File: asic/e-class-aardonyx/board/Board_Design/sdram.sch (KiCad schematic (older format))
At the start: 27 parts, among them J4 Conn_1x4, U2 IS42S32160F-TSOP2, U3 CDCE913PW, Y2 27MHz

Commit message: update bom
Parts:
- U2: Description (none) -> IC DRAM 512M PARALLEL 86TSOP II; Digikey PartNumber (none) -> 706-1417-5-ND; Manufactured Part Number (none) -> IS42S32160F-7TLI; Maufaturer (none) -> ISSI, Integrated Silicon Solution Inc
- U3: Description (none) -> IC PROG PLL VCXO CLK SYN 14TSSOP; Digikey PartNumber (none) -> 296-38908-1-ND; Manufactured Part Number (none) -> CDCE913PWR; Maufaturer (none) -> Texas Instruments
- Y2: Description (none) -> CRYSTAL 27.0000MHZ 18PF SMD; Digikey PartNumber (none) -> XC1002CT-ND; Manufactured Part Number (none) -> ECS-270-18-5PX-F-TR; Maufaturer (none) -> ECS Inc.
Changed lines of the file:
@@
 F 1 "IS42S32160F-TSOP2" H 3050 4800 50  0000 C CNN
 F 2 "" H 3100 4950 50  0001 C CNN
-F 3 "" H 3100 4950 50  0001 C CNN
+F 3 "https://www.digikey.in/product-detail/en/issi-integrated-silicon-solution-inc/IS42S32160F-7TLI/706-1417-5-ND/5319838" H 3100 4950 50  0001 C CNN
+F 4 "IC DRAM 512M PARALLEL 86TSOP II" H 3100 4800 50  0001 C CNN "Description"
+F 5 "706-1417-5-ND" H 3100 4800 50  0001 C CNN "Digikey PartNumber"
+F 6 "IS42S32160F-7TLI" H 3100 4800 50  0001 C CNN "Manufactured Part Number"
+F 7 "ISSI, Integrated Silicon Solution Inc" H 3100 4800 50  0001 C CNN "Maufaturer"
 	1    3100 4800
 	1    0    0    -1
@@
 F 1 "27MHz" H 8650 1500 50  0000 L CNN
 F 2 "" H 8750 1350 50  0001 C CNN
-F 3 "~" H 8750 1350 50  0001 C CNN
+F 3 "https://www.digikey.in/product-detail/en/ecs-inc/ECS-270-18-5PX-F-TR/XC1002CT-ND/813243" H 8750 1350 50  0001 C CNN
+F 4 "CRYSTAL 27.0000MHZ 18PF SMD" H 8750 1350 50  0001 C CNN "Description"
+F 5 "XC1002CT-ND" H 8750 1350 50  0001 C CNN "Digikey PartNumber"
+F 6 "ECS-270-18-5PX-F-TR" H 8750 1350 50  0001 C CNN "Manufactured Part Number"
+F 7 "ECS Inc." H 8750 1350 50  0001 C CNN "Maufaturer"
 	1    8750 1350
 	-1   0    0    1
@@
 F 1 "CDCE913PW" H 9150 1350 50  0000 C CNN
 F 2 "SOP65P640X120-14N" H 8750 2200 50  0001 L BNN
-F 3 "CDCE913PW" H 8750 2200 50  0001 L BNN
+F 3 "https://www.digikey.in/product-detail/en/texas-instruments/CDCE913PWR/296-38908-1-ND/5143014" H 8750 2200 50  0001 L BNN
 F 4 "58M0317" H 8750 2200 50  0001 L BNN "Field4"
 F 5 "TSSOP-14" H 8750 2200 50  0001 L BNN "Field5"
 F 6 "Texas Instruments" H 8750 2200 50  0001 L BNN "Field6"
 F 7 "1543748" H 8750 2200 50  0001 L BNN "Field7"
+F 8 "IC PROG PLL VCXO CLK SYN 14TSSOP" H 8750 2200 50  0001 C CNN "Description"
+F 9 "296-38908-1-ND" H 8750 2200 50  0001 C CNN "Digikey PartNumber"
+F 10 "CDCE913PWR" H 8750 2200 50  0001 C CNN "Manufactured Part Number"
+F 11 "Texas Instruments" H 8750 2200 50  0001 C CNN "Maufaturer"
 	1    8750 2200
 	1    0    0    -1
@@
 F 1 "22E" V 9900 2750 50  0000 C CNN
 F 2 "" V 9990 2590 50  0001 C CNN
-F 3 "~" H 9950 2600 50  0001 C CNN
+F 3 "" H 9950 2600 50  0001 C CNN
 	1    9950 2600
 	0    1    1    0

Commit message: update BOM
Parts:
- C18, C19, C20, C21, C22, C23, C24, C25, C26, C27, C28, C29, C30, C31, C32: Description CAP CER 0.1UF 16V X7R 0402 -> CAP CER 0.1UF 25V X7R 0402; Digikey PartNumber 490-6328-1-ND -> 478-10050-1-ND; Manufactured Part Number GRM155R71C104KA88J -> 04023C104JAT2A; Maufaturer Murata -> AVX Corporation
- R24: Description (none) -> RES SMD 22 OHM 1% 1/16W 0402; Digikey PartNumber (none) -> 311-22.0LRCT-ND; Manufactured Part Number (none) -> RC0402FR-0722RL; Maufaturer (none) -> Yageo

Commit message: updated BOM
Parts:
- C18, C19, C20, C21, C22, C23, C24, C25, C26, C27, C28, C29: value 0.1uF -> 0.1UF,0402
- C30, C31, C32: value 0.1uf -> 0.1UF,0402
- J4: Description (none) -> CONN HEADER VERT 4POS 2.54MM; Digikey PartNumber (none) -> 609-3262-ND; Manufactured Part Number (none) -> 68000-404HLF; Maufaturer (none) -> Amphenol ICC (FCI)
- R19, R20, R21, R22, R23: value 4.7K -> 4.7KE, 0402
- R24: value 22E -> 22E,0402
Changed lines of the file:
@@
 EESchema Schematic File Version 4
-EELAYER 30 0
+LIBS:Aardonyx-cache
+EELAYER 29 0
 EELAYER END
 $Descr A4 11693 8268
@@
 P 1650 1400
 F 0 "C18" H 1650 1500 50  0000 L CNN
-F 1 "0.1uF" H 1650 1300 50  0000 L CNN
+F 1 "0.1UF,0402" H 1650 1300 50  0000 L CNN
 F 2 "" H 1650 1400 50  0001 C CNN
 F 3 "https://www.digikey.in/product-detail/en/avx-corporation/04023C104JAT2A/478-10050-1-ND/6564273" H 1650 1400 50  0001 C CNN
@@
 P 1900 1400
 F 0 "C19" H 1900 1500 50  0000 L CNN
-F 1 "0.1uF" H 1900 1300 50  0000 L CNN
+F 1 "0.1UF,0402" H 1900 1300 50  0000 L CNN
 F 2 "" H 1900 1400 50  0001 C CNN
 F 3 "https://www.digikey.in/product-detail/en/avx-corporation/04023C104JAT2A/478-10050-1-ND/6564273" H 1900 1400 50  0001 C CNN
@@
 P 2150 1400
 F 0 "C20" H 2150 1500 50  0000 L CNN
-F 1 "0.1uF" H 2150 1300 50  0000 L CNN
+F 1 "0.1UF,0402" H 2150 1300 50  0000 L CNN
 F 2 "" H 2150 1400 50  0001 C CNN
 F 3 "https://www.digikey.in/product-detail/en/avx-corporation/04023C104JAT2A/478-10050-1-ND/6564273" H 2150 1400 50  0001 C CNN
@@
 P 2400 1400
 F 0 "C21" H 2400 1500 50  0000 L CNN
-F 1 "0.1uF" H 2400 1300 50  0000 L CNN
+F 1 "0.1UF,0402" H 2400 1300 50  0000 L CNN
 F 2 "" H 2400 1400 50  0001 C CNN
 F 3 "https://www.digikey.in/product-detail/en/avx-corporation/04023C104JAT2A/478-10050-1-ND/6564273" H 2400 1400 50  0001 C CNN
@@
 P 2650 1400
 F 0 "C22" H 2650 1500 50  0000 L CNN
-F 1 "0.1uF" H 2650 1300 50  0000 L CNN
+F 1 "0.1UF,0402" H 2650 1300 50  0000 L CNN
 F 2 "" H 2650 1400 50  0001 C CNN
 F 3 "https://www.digikey.in/product-detail/en/avx-corporation/04023C104JAT2A/478-10050-1-ND/6564273" H 2650 1400 50  0001 C CNN
@@
 P 2900 1400
 F 0 "C23" H 2900 1500 50  0000 L CNN
-F 1 "0.1uF" H 2900 1300 50  0000 L CNN
+F 1 "0.1UF,0402" H 2900 1300 50  0000 L CNN
 F 2 "" H 2900 1400 50  0001 C CNN
 F 3 "https://www.digikey.in/product-detail/en/avx-corporation/04023C104JAT2A/478-10050-1-ND/6564273" H 2900 1400 50  0001 C CNN
@@
 P 3150 1400
 F 0 "C24" H 3150 1500 50  0000 L CNN
-F 1 "0.1uF" H 3150 1300 50  0000 L CNN
+F 1 "0.1UF,0402" H 3150 1300 50  0000 L CNN
 F 2 "" H 3150 1400 50  0001 C CNN
 F 3 "https://www.digikey.in/product-detail/en/avx-corporation/04023C104JAT2A/478-10050-1-ND/6564273" H 3150 1400 50  0001 C CNN
@@
 P 3400 1400
 F 0 "C25" H 3400 1500 50  0000 L CNN
-F 1 "0.1uF" H 3400 1300 50  0000 L CNN
+F 1 "0.1UF,0402" H 3400 1300 50  0000 L CNN
 F 2 "" H 3400 1400 50  0001 C CNN
 F 3 "https://www.digikey.in/product-detail/en/avx-corporation/04023C104JAT2A/478-10050-1-ND/6564273" H 3400 1400 50  0001 C CNN
@@
 P 3650 1400
 F 0 "C26" H 3650 1500 50  0000 L CNN
-F 1 "0.1uF" H 3650 1300 50  0000 L CNN
+F 1 "0.1UF,0402" H 3650 1300 50  0000 L CNN
 F 2 "" H 3650 1400 50  0001 C CNN
 F 3 "https://www.digikey.in/product-detail/en/avx-corporation/04023C104JAT2A/478-10050-1-ND/6564273" H 3650 1400 50  0001 C CNN
@@
 P 3900 1400
 F 0 "C27" H 3900 1500 50  0000 L CNN
-F 1 "0.1uF" H 3900 1300 50  0000 L CNN
+F 1 "0.1UF,0402" H 3900 1300 50  0000 L CNN
 F 2 "" H 3900 1400 50  0001 C CNN
 F 3 "https://www.digikey.in/product-detail/en/avx-corporation/04023C104JAT2A/478-10050-1-ND/6564273" H 3900 1400 50  0001 C CNN
@@
 P 4150 1400
 F 0 "C28" H 4150 1500 50  0000 L CNN
-F 1 "0.1uF" H 4150 1300 50  0000 L CNN
+F 1 "0.1UF,0402" H 4150 1300 50  0000 L CNN
 F 2 "" H 4150 1400 50  0001 C CNN
 F 3 "https://www.digikey.in/product-detail/en/avx-corporation/04023C104JAT2A/478-10050-1-ND/6564273" H 4150 1400 50  0001 C CNN
@@
 P 4400 1400
 F 0 "C29" H 4400 1500 50  0000 L CNN
-F 1 "0.1uF" H 4400 1300 50  0000 L CNN
+F 1 "0.1UF,0402" H 4400 1300 50  0000 L CNN
 F 2 "" H 4400 1400 50  0001 C CNN
 F 3 "https://www.digikey.in/product-detail/en/avx-corporation/04023C104JAT2A/478-10050-1-ND/6564273" H 4400 1400 50  0001 C CNN
@@
 AR Path="/5D8B37B8/5EFB4D01" Ref="R20"  Part="1"
 F 0 "R20" H 7150 2350 50  0000 L CNN
-F 1 "4.7K" H 7150 2050 50  0000 L CNN
+F 1 "4.7KE, 0402" H 7150 2050 50  0000 L CNN
 F 2 "" V 7190 2190 50  0001 C CNN
 F 3 "https://www.digikey.in/product-detail/en/yageo/RC0402JR-074K7L/311-4-7KJRTR-ND/726477" H 7150 2200 50  0001 C CNN
@@
 AR Path="/5D8B37B8/5EFB4D07" Ref="R19"  Part="1"
 F 0 "R19" H 6850 2350 50  0000 L CNN
-F 1 "4.7K" H 6850 2050 50  0000 L CNN
+F 1 "4.7KE, 0402" H 6850 2050 50  0000 L CNN
 F 2 "" V 6890 2190 50  0001 C CNN
 F 3 "https://www.digikey.in/product-detail/en/yageo/RC0402JR-074K7L/311-4-7KJRTR-ND/726477" H 6850 2200 50  0001 C CNN
@@
 AR Path="/5D8B37B8/5EFB4D13" Ref="C31"  Part="1"
 F 0 "C31" H 10000 2100 50  0000 L CNN
-F 1 "0.1uf" H 10000 1900 50  0000 L CNN
+F 1 "0.1UF,0402" H 10000 1900 50  0000 L CNN
 F 2 "" H 10000 2000 50  0001 C CNN
 F 3 "https://www.digikey.in/product-detail/en/avx-corporation/04023C104JAT2A/478-10050-1-ND/6564273" H 10000 2000 50  0001 C CNN
@@
 AR Path="/5D8B37B8/5EFB4D19" Ref="C32"  Part="1"
 F 0 "C32" H 10250 2100 50  0000 L CNN
-F 1 "0.1uf" H 10250 1900 50  0000 L CNN
+F 1 "0.1UF,0402" H 10250 1900 50  0000 L CNN
 F 2 "" H 10250 2000 50  0001 C CNN
 F 3 "https://www.digikey.in/product-detail/en/avx-corporation/04023C104JAT2A/478-10050-1-ND/6564273" H 10250 2000 50  0001 C CNN
@@
 AR Path="/5D8B37B8/5EFB4D80" Ref="R24"  Part="1"
 F 0 "R24" V 9900 2450 50  0000 C CNN
-F 1 "22E" V 9900 2750 50  0000 C CNN
+F 1 "22E,0402" V 9900 2750 50  0000 C CNN
 F 2 "" V 9990 2590 50  0001 C CNN
 F 3 "https://www.digikey.com/product-detail/en/yageo/RC0402FR-0722RL/311-22-0LRCT-ND/729509" H 9950 2600 50  0001 C CNN
@@
 AR Path="/5D8B37B8/5F80E136" Ref="R21"  Part="1"
 F 0 "R21" H 7400 2350 50  0000 L CNN
-F 1 "4.7K" H 7400 2100 50  0000 L CNN
+F 1 "4.7KE, 0402" H 7400 2100 50  0000 L CNN
 F 2 "" V 7440 2190 50  0001 C CNN
 F 3 "https://www.digikey.in/product-detail/en/yageo/RC0402JR-074K7L/311-4-7KJRTR-ND/726477" H 7400 2200 50  0001 C CNN
@@
 AR Path="/5D8B37B8/5F82D0FE" Ref="R23"  Part="1"
 F 0 "R23" H 7450 2800 50  0000 L CNN
-F 1 "4.7K" H 7650 2700 50  0000 L CNN
+F 1 "4.7KE, 0402" H 7650 2700 50  0000 L CNN
 F 2 "" V 7690 2790 50  0001 C CNN
 F 3 "https://www.digikey.in/product-detail/en/yageo/RC0402JR-074K7L/311-4-7KJRTR-ND/726477" H 7650 2800 50  0001 C CNN
@@
 AR Path="/5D8B37B8/5F8A4363" Ref="R22"  Part="1"
 F 0 "R22" H 7650 2150 50  0000 L CNN
-F 1 "4.7K" H 7700 1950 50  0000 L CNN
+F 1 "4.7KE, 0402" H 7700 1950 50  0000 L CNN
 F 2 "" V 7690 1990 50  0001 C CNN
 F 3 "https://www.digikey.in/product-detail/en/yageo/RC0402JR-074K7L/311-4-7KJRTR-ND/726477" H 7650 2000 50  0001 C CNN
@@
 AR Path="/5D8B37B8/5F8E5F7E" Ref="C30"  Part="1"
 F 0 "C30" H 7450 1650 50  0000 L CNN
-F 1 "0.1uf" H 7450 1450 50  0000 L CNN
+F 1 "0.1UF,0402" H 7450 1450 50  0000 L CNN
 F 2 "" H 7450 1550 50  0001 C CNN
 F 3 "https://www.digikey.in/product-detail/en/avx-corporation/04023C104JAT2A/478-10050-1-ND/6564273" H 7450 1550 50  0001 C CNN
@@
 F 1 "Conn_1x4" H 6200 2100 50  0000 L CNN
 F 2 "" H 6350 2450 50  0001 C CNN
-F 3 "~" H 6350 2450 50  0001 C CNN
+F 3 "https://www.digikey.com/product-detail/en/amphenol-icc-fci/68000-404HLF/609-3262-ND/1878463" H 6350 2450 50  0001 C CNN
+F 4 "CONN HEADER VERT 4POS 2.54MM" H 6350 2450 50  0001 C CNN "Description"
+F 5 "609-3262-ND" H 6350 2450 50  0001 C CNN "Digikey PartNumber"
+F 6 "68000-404HLF" H 6350 2450 50  0001 C CNN "Manufactured Part Number"
+F 7 "Amphenol ICC (FCI)" H 6350 2450 50  0001 C CNN "Maufaturer"
 	1    6350 2450
 	-1   0    0    -1

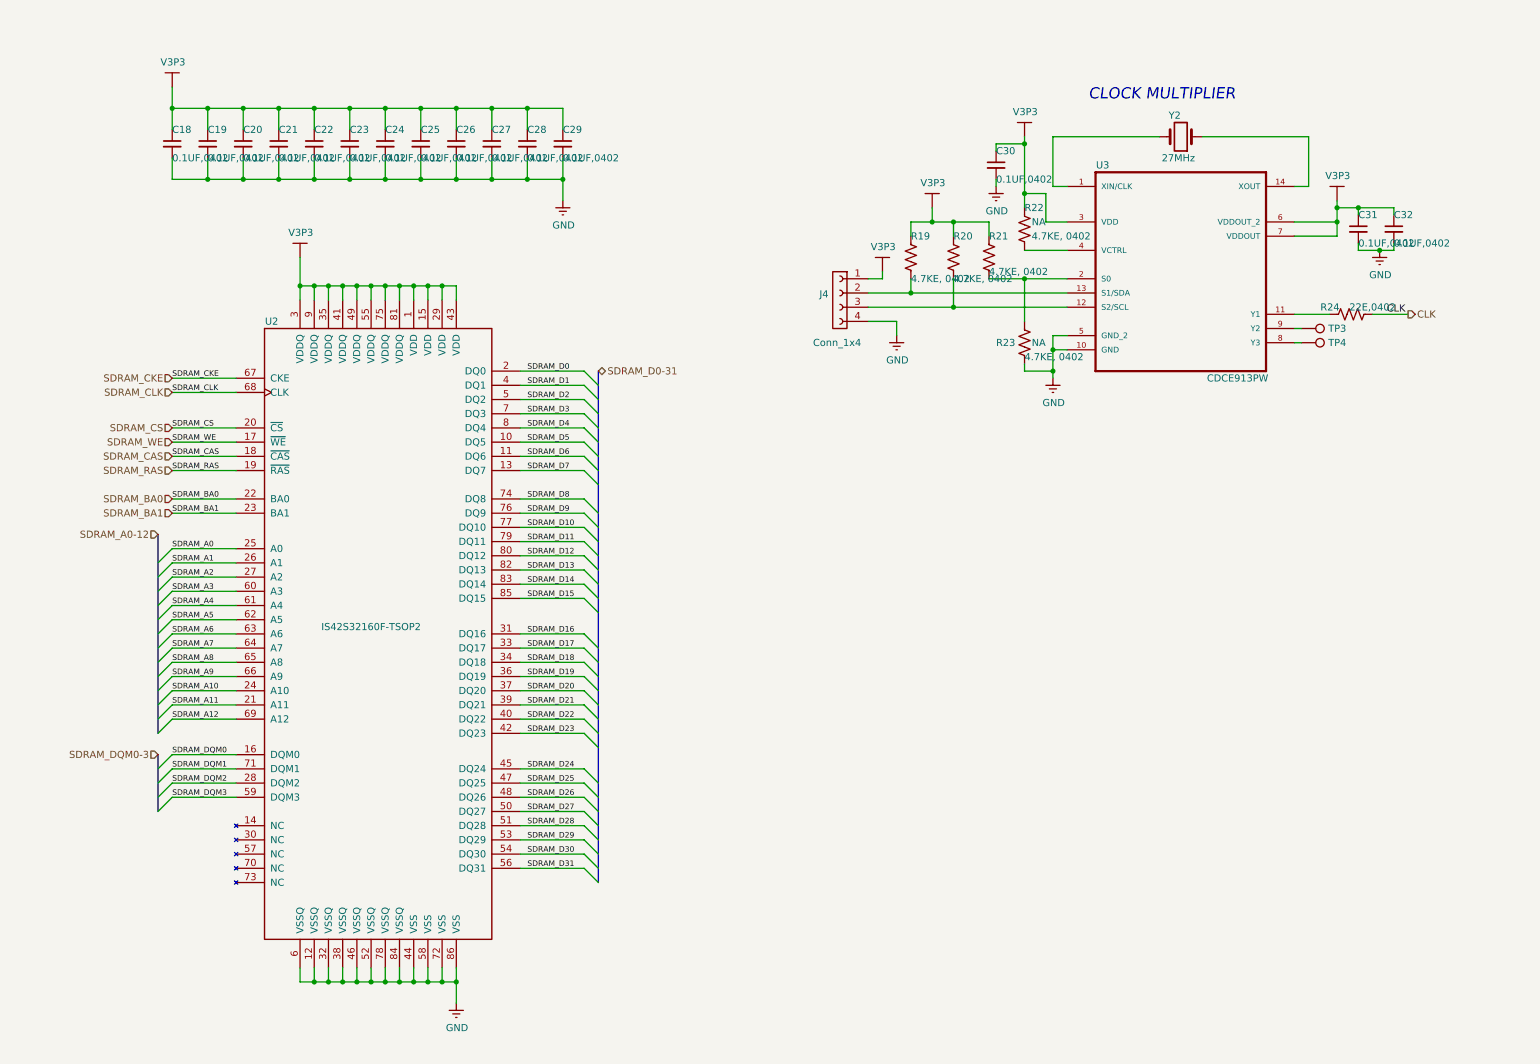
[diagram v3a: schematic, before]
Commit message: updated commented pending schematic
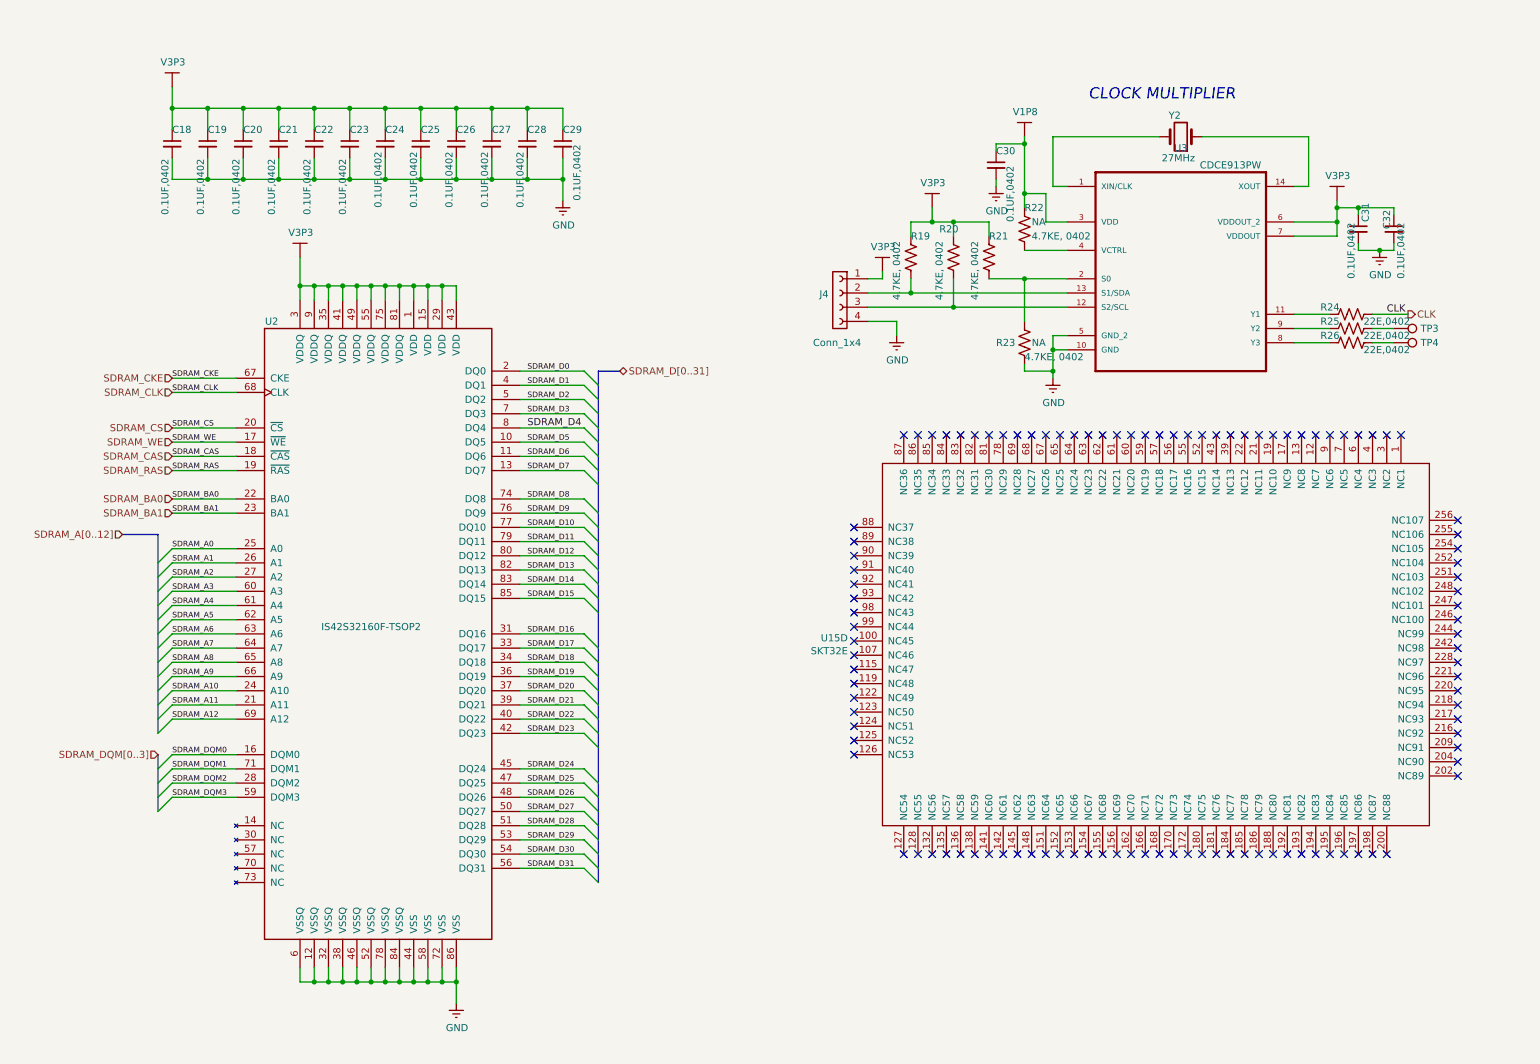
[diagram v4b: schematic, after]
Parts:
- removed U3: CDCE913PW, SOP65P640X120-14N, symbol Aardonyx-rescue:CDCE913PW-aardonyx
- added R25, R26: 22E,0402, symbol Aardonyx-rescue:R_US-aardonyx
- added U15: SKT32E, symbol Aardonyx-rescue:SKT32E-skt32e_asic
- added U3: CDCE913PW, SOP65P640X120-14N, symbol Aardonyx-rescue:CDCE913PW-skt32e_asic
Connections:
- net GNDREF: now also U3.10 (GND), U3.5 (GND_2)
- net at TP3.1: now also R25.1
- net at TP4.1: now also R26.1
- net at J4.3 (Pin_3), R20.2: now also U3.12 (S2/SCL)
- net at J4.2 (Pin_2), R19.2: now also U3.13 (S1/SDA)
- net at Y2.1: now also U3.14 (XOUT)
- net at Y2.2: now also U3.1 (XIN/CLK)
- net at C31.1, C32.1: now also U3.6 (VDDOUT_2), U3.7 (VDDOUT)
- net at R24.2: now also U3.11 (Y1)
- net at R21.2, R23.1: now also U3.2 (S0)
- net at C30.1, R22.1: now also U3.3 (VDD)
- net at R22.2: now also U3.4 (VCTRL)
- new net: R26.2, U3.8 (Y3)
- new net: R25.2, U3.9 (Y2)
- no-connect marks 0 -> 107
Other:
- moved on the sheet: TP3, TP4

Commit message: updated footprint for netlist
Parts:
- C18, C19, C20, C21, C22, C23, C24, C25, C26, C27, C28, C29, C30, C31, C32: footprint (none) -> Capacitor_SMD:C_0402_1005Metric
- R19, R20, R21, R22, R23, R24, R25, R26: footprint (none) -> Resistor_SMD:R_0402_1005Metric
- TP3, TP4: footprint (none) -> TestPoint:TestPoint_Bridge_Pitch2.54mm_Drill0.7mm
- U15: footprint (none) -> Aardonyx:SKT32E_IITM
- U3: footprint SOP65P640X120-14N -> Package_SO:TSSOP-14_4.4x5mm_P0.65mm
- Y2: footprint (none) -> Crystal:Crystal_SMD_HC49-SD_HandSoldering

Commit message: Updated schematic
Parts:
- U15: Description (none) -> E class Shakti Processor; Digikey PartNumber (none) -> NA; Manufactured Part Number (none) -> SKT32E; Maufaturer (none) -> SCL / IITM
- U3: Description (none) -> IC PROG PLL VCXO CLK SYN 14TSSOP; Digikey PartNumber (none) -> 296-38908-1-ND; Manufactured Part Number (none) -> CDCE913PWR; Maufaturer (none) -> Texas Instruments
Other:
- note added: "512Mb - SDRAM (16 x 32Mbit)"
- note added: "86-pin TSOP-ll"
- note added: "SKT32E - SDRAM INTERFACE\n"
- note added: "SKT32E NC PINS\n"
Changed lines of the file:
@@
 EESchema Schematic File Version 4
-EELAYER 30 0
+LIBS:Aardonyx-cache
+EELAYER 29 0
 EELAYER END
 $Descr A4 11693 8268
 encoding utf-8
 Sheet 3 7
-Title "AARDONYX_DEVELOPMENT_BOARD"
+Title "AARDONYX SKT32E DEVELOPMENT BOARD"
 Date ""
 Rev "R1V0"
@@
 Comment1 ""
 Comment2 ""
-Comment3 ""
-Comment4 ""
+Comment3 "SKT32E - Clock Multiplier"
+Comment4 "SKT32E - SDRAM Interface"
 $EndDescr
 $Comp
@@
 Text Label 10200 2600 0    50   ~ 0
 CLK
-Text Notes 8100 1100 0    79   Italic 0
+Text Notes 7300 900  0    200  ~ 40
 CLOCK MULTIPLIER\n
 Wire Wire Line
@@
 F 1 "CDCE913PW" H 9100 2850 50  0000 C CNN
 F 2 "Package_SO:TSSOP-14_4.4x5mm_P0.65mm" H 8900 2000 50  0001 L BNN
-F 3 "" H 8750 2200 50  0001 L BNN
+F 3 "https://www.digikey.com/product-detail/en/texas-instruments/CDCE913PWR/296-38908-1-ND/5143014" H 8750 2200 50  0001 L BNN
 F 4 "58M0317" H 8750 2200 50  0001 L BNN "Field4"
 F 5 "TSSOP-14" H 8750 2200 50  0001 L BNN "Field5"
 F 6 "Texas Instruments" H 8750 2200 50  0001 L BNN "Field6"
 F 7 "1543748" H 8750 2200 50  0001 L BNN "Field7"
+F 8 "	IC PROG PLL VCXO CLK SYN 14TSSOP" H 8750 2200 50  0001 C CNN "Description"
+F 9 "296-38908-1-ND" H 8750 2200 50  0001 C CNN "Digikey PartNumber"
+F 10 "CDCE913PWR" H 8750 2200 50  0001 C CNN "Manufactured Part Number"
+F 11 "	Texas Instruments" H 8750 2200 50  0001 C CNN "Maufaturer"
 	1    8750 2200
 	1    0    0    -1
@@
 U 4 1 5ED60D0C
 P 9100 4500
-F 0 "U15" V 9479 1806 50  0000 R CNN
-F 1 "SKT32E" V 9570 1806 50  0000 R CNN
+F 0 "U15" V 8200 5950 50  0000 R CNN
+F 1 "SKT32E" V 9100 4000 50  0000 R CNN
 F 2 "Aardonyx:SKT32E_IITM" H 8250 5900 50  0001 C CNN
-F 3 "" H 8250 5900 50  0001 C CNN
+F 3 "https://gitlab.com/shaktiproject/cores/shakti-soc/-/tree/master/asic/e-class-aardonyx" H 8250 5900 50  0001 C CNN
+F 4 "E class Shakti Processor" H 9100 4500 50  0001 C CNN "Description"
+F 5 "NA" H 9100 4500 50  0001 C CNN "Digikey PartNumber"
+F 6 "SKT32E" H 9100 4500 50  0001 C CNN "Manufactured Part Number"
+F 7 "SCL / IITM" H 9100 4500 50  0001 C CNN "Maufaturer"
 	4    9100 4500
 	0    1    1    0
@@
 	1    0    0    -1
 $EndComp
+Wire Notes Line
+	11200 3300 5950 3300
+Wire Notes Line
+	5950 500  5950 7800
+Text Notes 1250 800  0    200  ~ 40
+SKT32E - SDRAM INTERFACE\n
+Text Notes 7200 4950 0    200  ~ 40
+SKT32E NC PINS\n
 Wire Bus Line
 	1550 5700 1550 6100
@@
 Wire Bus Line
 	4650 3000 4650 6600
+Text Notes 4250 6950 0    50   ~ 0
+512Mb - SDRAM (16 x 32Mbit)
+Text Notes 4250 7100 0    50   ~ 0
+86-pin TSOP-ll
 $EndSCHEMATC
